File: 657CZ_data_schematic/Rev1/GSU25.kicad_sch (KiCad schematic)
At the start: 2 parts, among them J251 DE9_Socket, J252 DA15_Socket

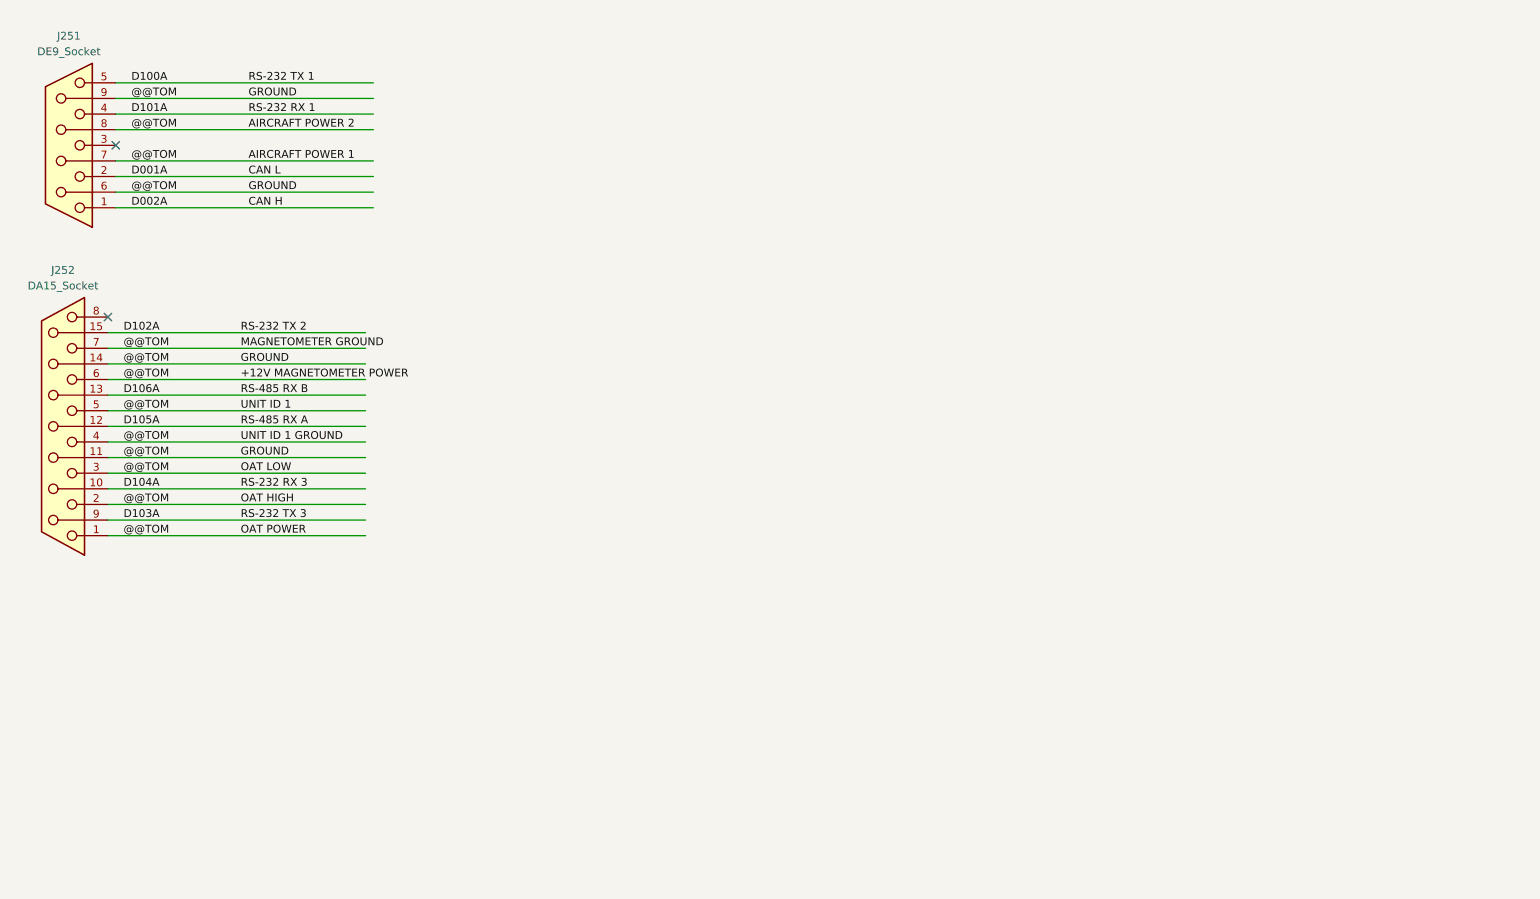
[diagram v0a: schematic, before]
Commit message: added data connections after AvClassics wiring. completed LRUs GMU, GDU, GSU, GAD, GNC, GTX, GTR  Not completed GMA, GEA and autopilot LRUs
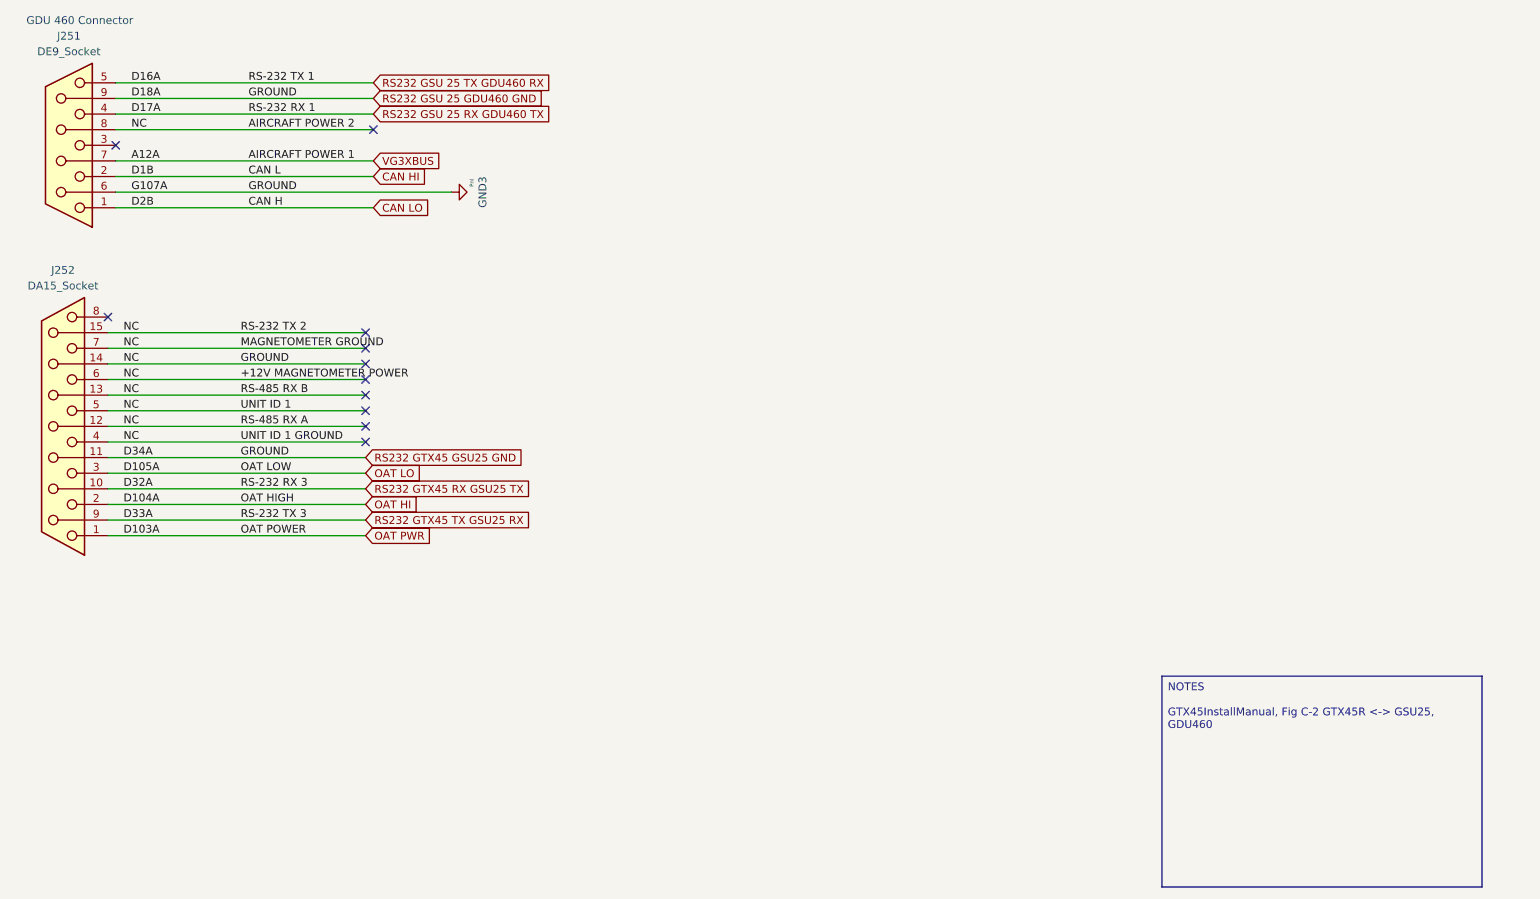
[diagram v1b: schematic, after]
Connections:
- net D102A is gone; now on net GND3: J252.15 (P15)
- net D105A is gone; now on net GND3: J252.12 (P12)
- net D106A is gone; now on net GND3: J252.13 (P13)
- net +12V MAGNETOMETER POWER renamed GND3
- net GND3: no longer J251.7, J252.1, J252.2, J252.3
- net CAN H renamed CAN LO
- net CAN L renamed CAN HI
- net D100A renamed RS232 GSU 25 TX GDU460 RX
- net D101A renamed RS232 GSU 25 RX GDU460 TX
- net D103A renamed RS232 GTX45 TX GSU25 RX
- net D104A renamed RS232 GTX45 RX GSU25 TX
- new net OAT HI: J252.2
- new net OAT LO: J252.3
- new net OAT PWR: J252.1
- new net VG3XBUS: J251.7
- no-connect marks 2 -> 11
